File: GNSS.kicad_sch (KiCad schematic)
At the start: 10 parts, among them J3 Conn_Coaxial, U5 NEO-M9N

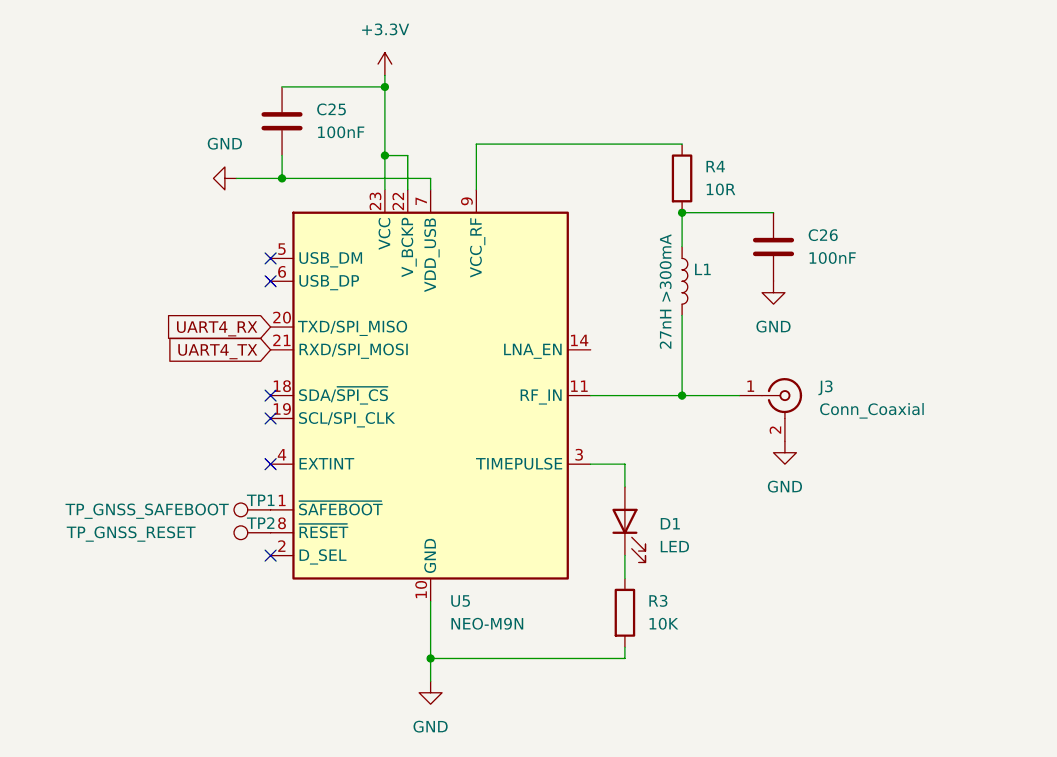
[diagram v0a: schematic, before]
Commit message: add sd card reader
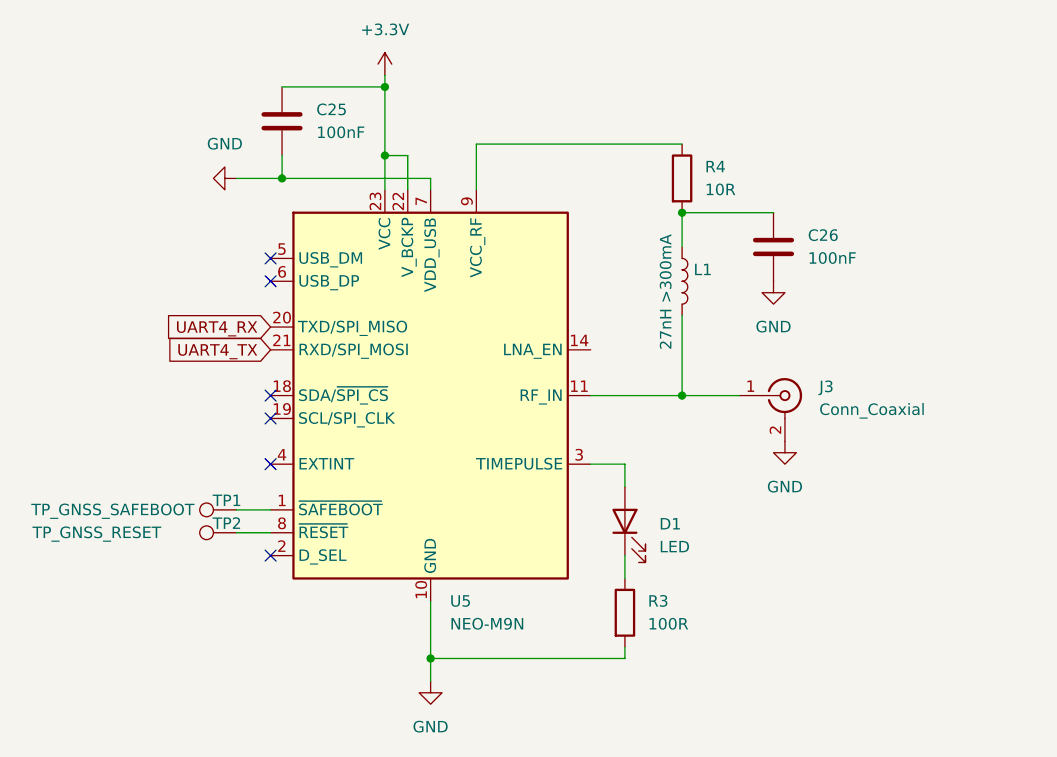
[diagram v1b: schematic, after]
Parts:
- R3: value 10K -> 100R
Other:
- moved on the sheet: TP1, TP2
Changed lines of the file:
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@@
+	(wire
+		(pts
+			(xy 116.84 107.95) (xy 120.65 107.95)
+		)
+		(stroke
+			(width 0)
+			(type default)
+		)
+	)
 	(wire
 		(pts
@@
 		(pts
 			(xy 135.89 68.58) (xy 133.35 68.58)
+		)
+		(stroke
+			(width 0)
+			(type default)
+		)
+	)
+	(wire
+		(pts
+			(xy 116.84 110.49) (xy 120.65 110.49)
 		)
 		(stroke
@@
 	(symbol
 		(lib_id "Connector:TestPoint")
-		(at 120.65 107.95 90)
+		(at 116.84 107.95 90)
 		(unit 1)
 		(exclude_from_sim no)
@@
 		(dnp no)
 		(property "Reference" "TP1"
-			(at 119.634 106.934 90)
+			(at 115.824 106.934 90)
 			(effects
 				(font
@@
 		)
 		(property "Value" "TP_GNSS_SAFEBOOT"
-			(at 106.934 107.95 90)
+			(at 103.124 107.95 90)
 			(effects
 				(font
@@
 		)
 		(property "Footprint" ""
-			(at 120.65 102.87 0)
+			(at 116.84 102.87 0)
 			(effects
 				(font
@@
 		)
 		(property "Datasheet" "~"
-			(at 120.65 102.87 0)
+			(at 116.84 102.87 0)
 			(effects
 				(font
@@
 		)
 		(property "Description" "test point"
-			(at 120.65 107.95 0)
+			(at 116.84 107.95 0)
 			(effects
 				(font
@@
 	(symbol
 		(lib_id "Connector:TestPoint")
-		(at 120.65 110.49 90)
+		(at 116.84 110.49 90)
 		(unit 1)
 		(exclude_from_sim no)
@@
 		(dnp no)
 		(property "Reference" "TP2"
-			(at 119.634 109.474 90)
+			(at 115.824 109.474 90)
 			(effects
 				(font
@@
 		)
 		(property "Value" "TP_GNSS_RESET"
-			(at 105.156 110.49 90)
+			(at 101.346 110.49 90)
 			(effects
 				(font
@@
 		)
 		(property "Footprint" ""
-			(at 120.65 105.41 0)
+			(at 116.84 105.41 0)
 			(effects
 				(font
@@
 		)
 		(property "Datasheet" "~"
-			(at 120.65 105.41 0)
+			(at 116.84 105.41 0)
 			(effects
 				(font
@@
 		)
 		(property "Description" "test point"
-			(at 120.65 110.49 0)
+			(at 116.84 110.49 0)
 			(effects
 				(font
@@
 			)
 		)
-		(property "Value" "10K"
+		(property "Value" "100R"
 			(at 162.56 120.6499 0)
 			(effects

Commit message: "Update KiRA Flight Computer schematic and PCB files"
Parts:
- removed TP1: TP_GNSS_SAFEBOOT, symbol Connector:TestPoint
- removed TP2: TP_GNSS_RESET, symbol Connector:TestPoint
- added J9: Conn_01x02_Pin, Connector_PinHeader_2.54mm:PinHeader_1x02_P2.54mm_Vertical, symbol Connector:Conn_01x02_Pin
- C25, C26: footprint (none) -> Capacitor_SMD:C_0603_1608Metric
- D1: value LED -> LED_GREEN; footprint (none) -> LED_SMD:LED_0603_1608Metric
- J3: footprint (none) -> Connector_Coaxial:BNC_Amphenol_B6252HB-NPP3G-50_Horizontal
- L1: footprint (none) -> Inductor_SMD:L_0603_1608Metric
- R3: value 100R -> 220R; footprint (none) -> Resistor_SMD:R_0402_1005Metric
- R4: footprint (none) -> Resistor_SMD:R_0402_1005Metric
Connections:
- net at U5.1 (~{SAFEBOOT}): now also J9.1 (Pin_1)
- net at U5.8 (~{RESET}): now also J9.2 (Pin_2)
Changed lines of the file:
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@@
-	)
-	(symbol
-		(lib_id "Connector:TestPoint")
-		(at 116.84 107.95 90)
-		(unit 1)
-		(exclude_from_sim no)
-		(in_bom yes)
-		(on_board yes)
-		(dnp no)
-		(property "Reference" "TP1"
-			(at 115.824 106.934 90)
-			(effects
-				(font
-					(size 1.27 1.27)
-				)
-			)
-		)
-		(property "Value" "TP_GNSS_SAFEBOOT"
-			(at 103.124 107.95 90)
-			(effects
-				(font
-					(size 1.27 1.27)
-				)
-			)
-		)
-		(property "Footprint" ""
-			(at 116.84 102.87 0)
-			(effects
-				(font
-					(size 1.27 1.27)
-				)
-				(hide yes)
-			)
-		)
-		(property "Datasheet" "~"
-			(at 116.84 102.87 0)
-			(effects
-				(font
-					(size 1.27 1.27)
-				)
-				(hide yes)
-			)
-		)
-		(property "Description" "test point"
-			(at 116.84 107.95 0)
-			(effects
-				(font
-					(size 1.27 1.27)
-				)
-				(hide yes)
-			)
-		)
-		(pin "1"
-		)
-		(instances
-			(project "KiRA Flight Computer"
-				(path "/aff8106b-a9b7-4e48-85ad-25b2eb3ce379/f42f4972-519d-4306-8fa1-8314a04aa80d"
-					(reference "TP1")
-					(unit 1)
-				)
-			)
-		)
 	)
 	(symbol
@@
 			)
 		)
-		(property "Value" "LED"
+		(property "Value" "LED_GREEN"
 			(at 163.83 112.0774 90)
 			(effects
@@
 			)
 		)
-		(property "Footprint" ""
+		(property "Footprint" "LED_SMD:LED_0603_1608Metric"
 			(at 160.02 109.22 0)
 			(effects
@@
 	)
 	(symbol
-		(lib_id "Connector:TestPoint")
-		(at 116.84 110.49 90)
-		(unit 1)
-		(exclude_from_sim no)
-		(in_bom yes)
-		(on_board yes)
-		(dnp no)
-		(property "Reference" "TP2"
-			(at 115.824 109.474 90)
-			(effects
-				(font
-					(size 1.27 1.27)
-				)
-			)
-		)
-		(property "Value" "TP_GNSS_RESET"
-			(at 101.346 110.49 90)
-			(effects
-				(font
-					(size 1.27 1.27)
-				)
-			)
-		)
-		(property "Footprint" ""
-			(at 116.84 105.41 0)
-			(effects
-				(font
-					(size 1.27 1.27)
-				)
-				(hide yes)
-			)
-		)
-		(property "Datasheet" "~"
-			(at 116.84 105.41 0)
-			(effects
-				(font
-					(size 1.27 1.27)
-				)
-				(hide yes)
-			)
-		)
-		(property "Description" "test point"
-			(at 116.84 110.49 0)
-			(effects
-				(font
-					(size 1.27 1.27)
-				)
-				(hide yes)
-			)
-		)
-		(pin "1"
-		)
-		(instances
-			(project "KiRA Flight Computer"
-				(path "/aff8106b-a9b7-4e48-85ad-25b2eb3ce379/f42f4972-519d-4306-8fa1-8314a04aa80d"
-					(reference "TP2")
-					(unit 1)
-				)
-			)
-		)
-	)
-	(symbol
 		(lib_id "RF_GPS:NEO-M9N")
 		(at 138.43 95.25 0)
@@
 			)
 		)
-		(property "Footprint" ""
+		(property "Footprint" "Inductor_SMD:L_0603_1608Metric"
 			(at 166.37 82.55 0)
 			(effects
@@
 			)
 		)
-		(property "Footprint" ""
+		(property "Footprint" "Connector_Coaxial:BNC_Amphenol_B6252HB-NPP3G-50_Horizontal"
 			(at 177.8 95.25 0)
 			(effects
@@
 			)
 		)
-		(property "Footprint" ""
+		(property "Footprint" "Capacitor_SMD:C_0603_1608Metric"
 			(at 177.4952 82.55 0)
 			(effects
@@
 			)
 		)
-		(property "Footprint" ""
+		(property "Footprint" "Capacitor_SMD:C_0603_1608Metric"
 			(at 122.8852 68.58 0)
 			(effects
@@
 	)
 	(symbol
+		(lib_id "Connector:Conn_01x02_Pin")
+		(at 111.76 107.95 0)
+		(unit 1)
+		(exclude_from_sim no)
+		(in_bom yes)
+		(on_board yes)
+		(dnp no)
+		(property "Reference" "J9"
+			(at 102.87 106.934 0)
+			(effects
+				(font
+					(size 1.27 1.27)
+				)
+			)
+		)
+		(property "Value" "Conn_01x02_Pin"
+			(at 102.108 110.49 0)
+			(effects
+				(font
+					(size 1.27 1.27)
+				)
+			)
+		)
+		(property "Footprint" "Connector_PinHeader_2.54mm:PinHeader_1x02_P2.54mm_Vertical"
+			(at 111.76 107.95 0)
+			(effects
+				(font
+					(size 1.27 1.27)
+				)
+				(hide yes)
+			)
+		)
+		(property "Datasheet" "~"
+			(at 111.76 107.95 0)
+			(effects
+				(font
+					(size 1.27 1.27)
+				)
+				(hide yes)
+			)
+		)
+		(property "Description" "Generic connector, single row, 01x02, script generated"
+			(at 111.76 107.95 0)
+			(effects
+				(font
+					(size 1.27 1.27)
+				)
+				(hide yes)
+			)
+		)
+		(pin "1"
+		)
+		(pin "2"
+		)
+		(instances
+			(project ""
+				(path "/aff8106b-a9b7-4e48-85ad-25b2eb3ce379/f42f4972-519d-4306-8fa1-8314a04aa80d"
+					(reference "J9")
+					(unit 1)
+				)
+			)
+		)
+	)
+	(symbol
 		(lib_id "Device:R")
 		(at 160.02 119.38 0)
@@
 			)
 		)
-		(property "Value" "100R"
+		(property "Value" "220R"
 			(at 162.56 120.6499 0)
 			(effects
@@
 			)
 		)
-		(property "Footprint" ""
+		(property "Footprint" "Resistor_SMD:R_0402_1005Metric"
 			(at 158.242 119.38 90)
 			(effects
@@
 			)
 		)
-		(property "Footprint" ""
+		(property "Footprint" "Resistor_SMD:R_0402_1005Metric"
 			(at 164.592 71.12 90)
 			(effects

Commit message: Update PCB
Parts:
- added C37: 100nF, Capacitor_SMD:C_0603_1608Metric, symbol Device:C
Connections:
- net +3.3V: now also C37.1
- net GND: now also C37.2
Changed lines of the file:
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@@
+	)
+	(junction
+		(at 121.92 60.96)
+		(diameter 0)
+		(color 0 0 0 0)
 	)
 	(junction
@@
 	)
 	(junction
+		(at 109.22 71.12)
+		(diameter 0)
+		(color 0 0 0 0)
+	)
+	(junction
 		(at 133.35 60.96)
 		(diameter 0)
@@
 	(wire
 		(pts
+			(xy 109.22 71.12) (xy 121.92 71.12)
+		)
+		(stroke
+			(width 0)
+			(type default)
+		)
+	)
+	(wire
+		(pts
 			(xy 116.84 107.95) (xy 120.65 107.95)
 		)
@@
 	(wire
 		(pts
+			(xy 109.22 68.58) (xy 109.22 71.12)
+		)
+		(stroke
+			(width 0)
+			(type default)
+		)
+	)
+	(wire
+		(pts
 			(xy 156.21 95.25) (xy 166.37 95.25)
 		)
@@
 	(wire
 		(pts
-			(xy 116.84 71.12) (xy 121.92 71.12)
+			(xy 109.22 60.96) (xy 121.92 60.96)
+		)
+		(stroke
+			(width 0)
+			(type default)
+		)
+	)
+	(wire
+		(pts
+			(xy 101.6 71.12) (xy 109.22 71.12)
 		)
 		(stroke
@@
 	(symbol
 		(lib_id "power:GND")
-		(at 116.84 71.12 270)
+		(at 101.6 71.12 270)
 		(unit 1)
 		(exclude_from_sim no)
@@
 		(fields_autoplaced yes)
 		(property "Reference" "#PWR036"
-			(at 110.49 71.12 0)
+			(at 95.25 71.12 0)
 			(effects
 				(font
@@
 		)
 		(property "Value" "GND"
-			(at 115.57 67.31 90)
+			(at 100.33 67.31 90)
 			(effects
 				(font
@@
 		)
 		(property "Footprint" ""
-			(at 116.84 71.12 0)
+			(at 101.6 71.12 0)
 			(effects
 				(font
@@
 		)
 		(property "Datasheet" ""
-			(at 116.84 71.12 0)
+			(at 101.6 71.12 0)
 			(effects
 				(font
@@
 		)
 		(property "Description" "Power symbol creates a global label with name \"GND\" , ground"
-			(at 116.84 71.12 0)
+			(at 101.6 71.12 0)
 			(effects
 				(font
@@
 					(unit 1)
 				)
+			)
+		)
+	)
+	(symbol
+		(lib_id "Device:C")
+		(at 109.22 64.77 0)
+		(unit 1)
+		(exclude_from_sim no)
+		(in_bom yes)
+		(on_board yes)
+		(dnp no)
+		(fields_autoplaced yes)
+		(property "Reference" "C37"
+			(at 113.03 63.4999 0)
+			(effects
+				(font
+					(size 1.27 1.27)
+				)
+				(justify left)
+			)
+		)
+		(property "Value" "100nF"
+			(at 113.03 66.0399 0)
+			(effects
+				(font
+					(size 1.27 1.27)
+				)
+				(justify left)
+			)
+		)
+		(property "Footprint" "Capacitor_SMD:C_0603_1608Metric"
+			(at 110.1852 68.58 0)
+			(effects
+				(font
+					(size 1.27 1.27)
+				)
+				(hide yes)
+			)
+		)
+		(property "Datasheet" "~"
+			(at 109.22 64.77 0)
+			(effects
+				(font
+					(size 1.27 1.27)
+				)
+				(hide yes)
+			)
+		)
+		(property "Description" "Unpolarized capacitor"
+			(at 109.22 64.77 0)
+			(effects
+				(font
+					(size 1.27 1.27)
+				)
+				(hide yes)
+			)
+		)
+		(pin "1"
+		)
+		(pin "2"
+		)
+		(instances
+			(project "KiRA Flight Computer"
+				(path "/aff8106b-a9b7-4e48-85ad-25b2eb3ce379/f42f4972-519d-4306-8fa1-8314a04aa80d"
+					(reference "C37")
+					(unit 1)
+				)

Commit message: Update PCB
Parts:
- removed J3: Conn_Coaxial, Connector_Coaxial:BNC_Amphenol_B6252HB-NPP3G-50_Horizontal, symbol Connector:Conn_Coaxial
- removed J9: Conn_01x02_Pin, Connector_PinHeader_2.54mm:PinHeader_1x02_P2.54mm_Vertical, symbol Connector:Conn_01x02_Pin
- added J7: Conn_01x03, dep:CONSMA001SMDG, symbol Connector_Generic:Conn_01x03
- added R20, R21: R, Resistor_SMD:R_0402_1005Metric, symbol Device:R
- R4: footprint Resistor_SMD:R_0402_1005Metric -> Resistor_SMD:R_0603_1608Metric
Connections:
- net GND: now also J7.1 (Pin_1), J7.2 (Pin_2), R20.2, R21.2
- net at U5.1 (~{SAFEBOOT}): now also R20.1
- net at L1.2, U5.11 (RF_IN): now also J7.3 (Pin_3)
- net at U5.8 (~{RESET}): now also R21.1
- net at R4.1, U5.9 (VCC_RF): now also C26.1
- net at L1.1, R4.2: no longer C26.1
- net UART4_RX renamed UART2_RX
- net UART4_TX renamed UART2_TX

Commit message: questionable changes
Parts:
- removed J7: Conn_01x03, dep:CONSMA001SMDG, symbol Connector_Generic:Conn_01x03
- added J15: Conn_Coaxial, Connector_Coaxial:U.FL_Hirose_U.FL-R-SMT-1_Vertical, symbol Connector:Conn_Coaxial
- C37: value 100nF -> 1uF
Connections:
- net GND: now also J15.2 (Ext)
- net at L1.2, U5.11 (RF_IN): now also J15.1 (In)
- net at R4.1, U5.9 (VCC_RF): no longer C26.1
- net at L1.1, R4.2: now also C26.1
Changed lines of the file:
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@@
 	(paper "A4")
-	(junction
-		(at 177.8 92.71)
-		(diameter 0)
-		(color 0 0 0 0)
-	)
 	(junction
 		(at 109.22 118.11)
@@
 	)
 	(junction
-		(at 166.37 67.31)
-		(diameter 0)
-		(color 0 0 0 0)
-	)
-	(junction
 		(at 109.22 71.12)
 		(diameter 0)
@@
 		(color 0 0 0 0)
 	)
+	(junction
+		(at 166.37 74.93)
+		(diameter 0)
+		(color 0 0 0 0)
+	)
 	(no_connect
 		(at 120.65 95.25)
@@
 	(wire
 		(pts
-			(xy 177.8 92.71) (xy 181.61 92.71)
-		)
-		(stroke
-			(width 0)
-			(type default)
-		)
-	)
-	(wire
-		(pts
 			(xy 166.37 95.25) (xy 181.61 95.25)
 		)
@@
 	(wire
 		(pts
-			(xy 177.8 100.33) (xy 177.8 92.71)
-		)
-		(stroke
-			(width 0)
-			(type default)
-		)
-	)
-	(wire
-		(pts
 			(xy 118.11 118.11) (xy 118.11 110.49)
 		)
@@
 	(wire
 		(pts
-			(xy 177.8 90.17) (xy 181.61 90.17)
-		)
-		(stroke
-			(width 0)
-			(type default)
-		)
-	)
-	(wire
-		(pts
 			(xy 135.89 72.39) (xy 135.89 68.58)
 		)
@@
 	(wire
 		(pts
-			(xy 177.8 92.71) (xy 177.8 90.17)
-		)
-		(stroke
-			(width 0)
-			(type default)
-		)
-	)
-	(wire
-		(pts
-			(xy 176.53 67.31) (xy 176.53 74.93)
-		)
-		(stroke
-			(width 0)
-			(type default)
-		)
-	)
-	(wire
-		(pts
 			(xy 109.22 124.46) (xy 138.43 124.46)
 		)
@@
 	(wire
 		(pts
-			(xy 166.37 67.31) (xy 176.53 67.31)
+			(xy 166.37 74.93) (xy 176.53 74.93)
 		)
 		(stroke
@@
 	(symbol
 		(lib_id "power:GND")
-		(at 177.8 100.33 0)
+		(at 186.69 100.33 0)
 		(unit 1)
 		(exclude_from_sim no)
@@
 		(fields_autoplaced yes)
 		(property "Reference" "#PWR037"
-			(at 177.8 106.68 0)
+			(at 186.69 106.68 0)
 			(effects
 				(font
@@
 		)
 		(property "Value" "GND"
-			(at 177.8 105.41 0)
+			(at 186.69 105.41 0)
 			(effects
 				(font
@@
 		)
 		(property "Footprint" ""
-			(at 177.8 100.33 0)
+			(at 186.69 100.33 0)
 			(effects
 				(font
@@
 		)
 		(property "Datasheet" ""
-			(at 177.8 100.33 0)
+			(at 186.69 100.33 0)
 			(effects
 				(font
@@
 		)
 		(property "Description" "Power symbol creates a global label with name \"GND\" , ground"
-			(at 177.8 100.33 0)
+			(at 186.69 100.33 0)
 			(effects
 				(font
@@
 			)
 		)
-		(property "Value" "100nF"
+		(property "Value" "1uF"
 			(at 113.03 66.0399 0)
 			(effects
@@
 	)
 	(symbol
-		(lib_id "Connector_Generic:Conn_01x03")
-		(at 186.69 92.71 0)
-		(unit 1)
-		(exclude_from_sim no)
-		(in_bom yes)
-		(on_board yes)
-		(dnp no)
-		(fields_autoplaced yes)
-		(property "Reference" "J7"
-			(at 189.23 91.4399 0)
-			(effects
-				(font
-					(size 1.27 1.27)
-				)
-				(justify left)
-			)
-		)
-		(property "Value" "Conn_01x03"
-			(at 189.23 93.9799 0)
-			(effects
-				(font
-					(size 1.27 1.27)
-				)
-				(justify left)
-			)
-		)
-		(property "Footprint" "dep:CONSMA001SMDG"
-			(at 186.69 92.71 0)
-			(effects
-				(font
-					(size 1.27 1.27)
-				)
-				(hide yes)
-			)
-		)
-		(property "Datasheet" "~"
-			(at 186.69 92.71 0)
-			(effects
-				(font
-					(size 1.27 1.27)
-				)
-				(hide yes)
-			)
-		)
-		(property "Description" "Generic connector, single row, 01x03, script generated (kicad-library-utils/schlib/autogen/connector/)"
-			(at 186.69 92.71 0)
-			(effects
-				(font
-					(size 1.27 1.27)
-				)
-				(hide yes)
-			)
-		)
-		(pin "2"
-		)
-		(pin "1"
-		)
-		(pin "3"
-		)
-		(instances
-			(project ""
-				(path "/aff8106b-a9b7-4e48-85ad-25b2eb3ce379/f42f4972-519d-4306-8fa1-8314a04aa80d"
-					(reference "J7")
-					(unit 1)
-				)
-			)
-		)
-	)
-	(symbol
 		(lib_id "Device:R")
 		(at 166.37 71.12 0)
@@
 					(unit 1)
 				)
+			)
+		)
+	)
+	(symbol
+		(lib_id "Connector:Conn_Coaxial")
+		(at 186.69 95.25 0)
+		(unit 1)
+		(exclude_from_sim no)
+		(in_bom yes)
+		(on_board yes)
+		(dnp no)
+		(fields_autoplaced yes)
+		(property "Reference" "J15"
+			(at 190.5 94.2731 0)
+			(effects
+				(font
+					(size 1.27 1.27)
+				)
+				(justify left)
+			)
+		)
+		(property "Value" "Conn_Coaxial"
+			(at 190.5 96.8131 0)
+			(effects
+				(font
+					(size 1.27 1.27)
+				)
+				(justify left)
+			)
+		)
+		(property "Footprint" "Connector_Coaxial:U.FL_Hirose_U.FL-R-SMT-1_Vertical"
+			(at 186.69 95.25 0)
+			(effects
+				(font
+					(size 1.27 1.27)
+				)
+				(hide yes)
+			)
+		)
+		(property "Datasheet" "~"
+			(at 186.69 95.25 0)
+			(effects
+				(font
+					(size 1.27 1.27)
+				)
+				(hide yes)
+			)
+		)
+		(property "Description" "coaxial connector (BNC, SMA, SMB, SMC, Cinch/RCA, LEMO, ...)"
+			(at 186.69 95.25 0)
+			(effects
+				(font
+					(size 1.27 1.27)
+				)
+				(hide yes)
+			)
+		)
+		(pin "2"
+		)
+		(pin "1"
+		)
+		(instances
+			(project ""
+				(path "/aff8106b-a9b7-4e48-85ad-25b2eb3ce379/f42f4972-519d-4306-8fa1-8314a04aa80d"
+					(reference "J15")
+					(unit 1)
+				)

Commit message: PCB Update
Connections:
- net UART2_RX renamed UART3_RX
- net UART2_TX renamed UART3_TX
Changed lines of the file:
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@@
 		)
 	)
-	(global_label "UART2_TX"
+	(global_label "UART3_TX"
 		(shape input)
 		(at 120.65 90.17 180)
@@
 		)
 	)
-	(global_label "UART2_RX"
+	(global_label "UART3_RX"
 		(shape input)
 		(at 120.65 87.63 180)
